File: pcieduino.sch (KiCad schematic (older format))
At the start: 32 parts, among them IC1 ATMEGA328P-A, J1 PCIE-MINI, J2 ANALOG, J3 ISP, J4 POWER, J5 DIGITAL, SW1 SW_PUSH, U1 MCP2200, X1 12MHz, X2 8MHz

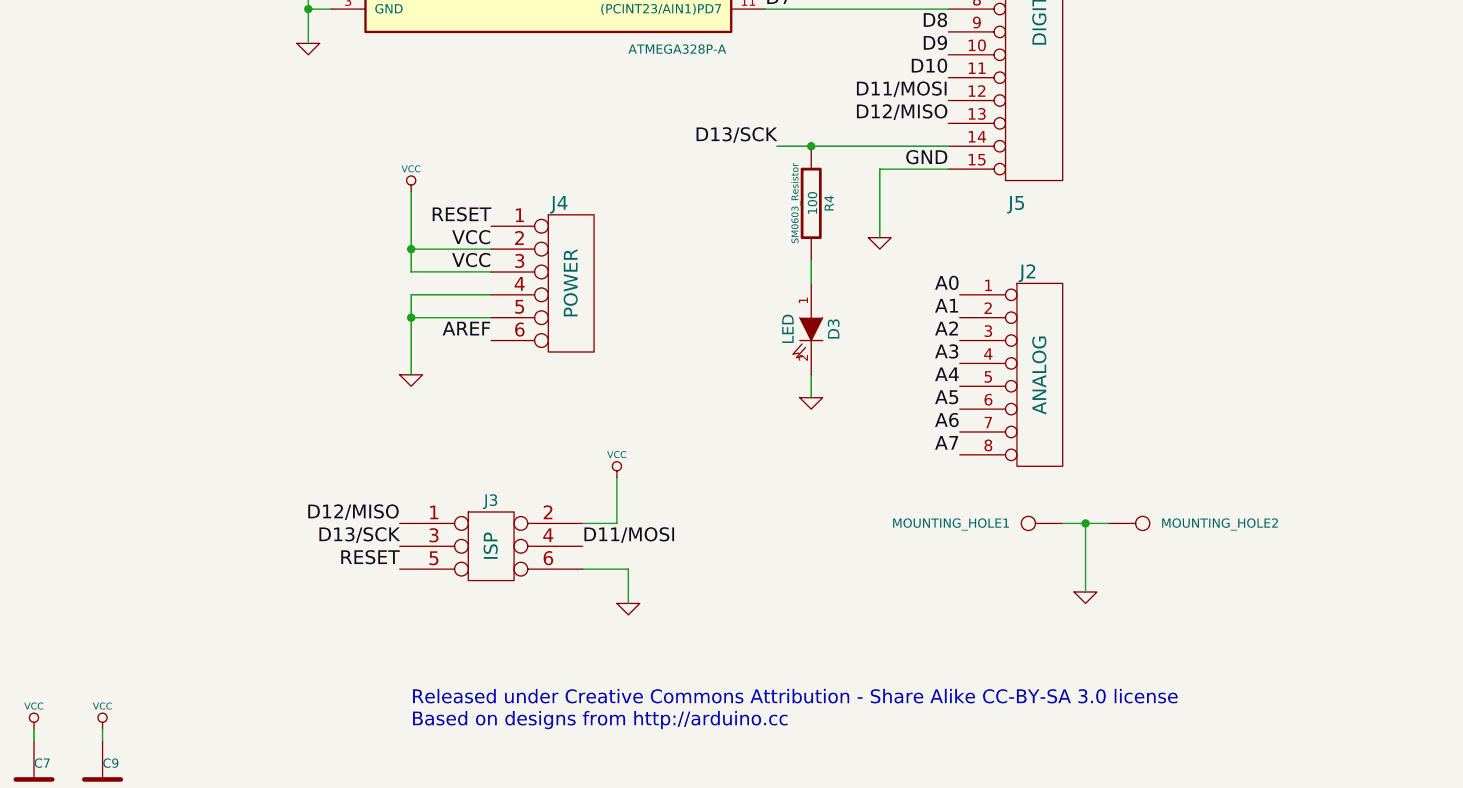
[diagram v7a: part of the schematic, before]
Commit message: add 01/04 changes
summary:

* redrawn the board starting from x=100.00, y=100.00 to have fix positioning
* combine analog and power headers
* remove RESET from power header because it already exists elsewhere
* redraw fill zones with duplication
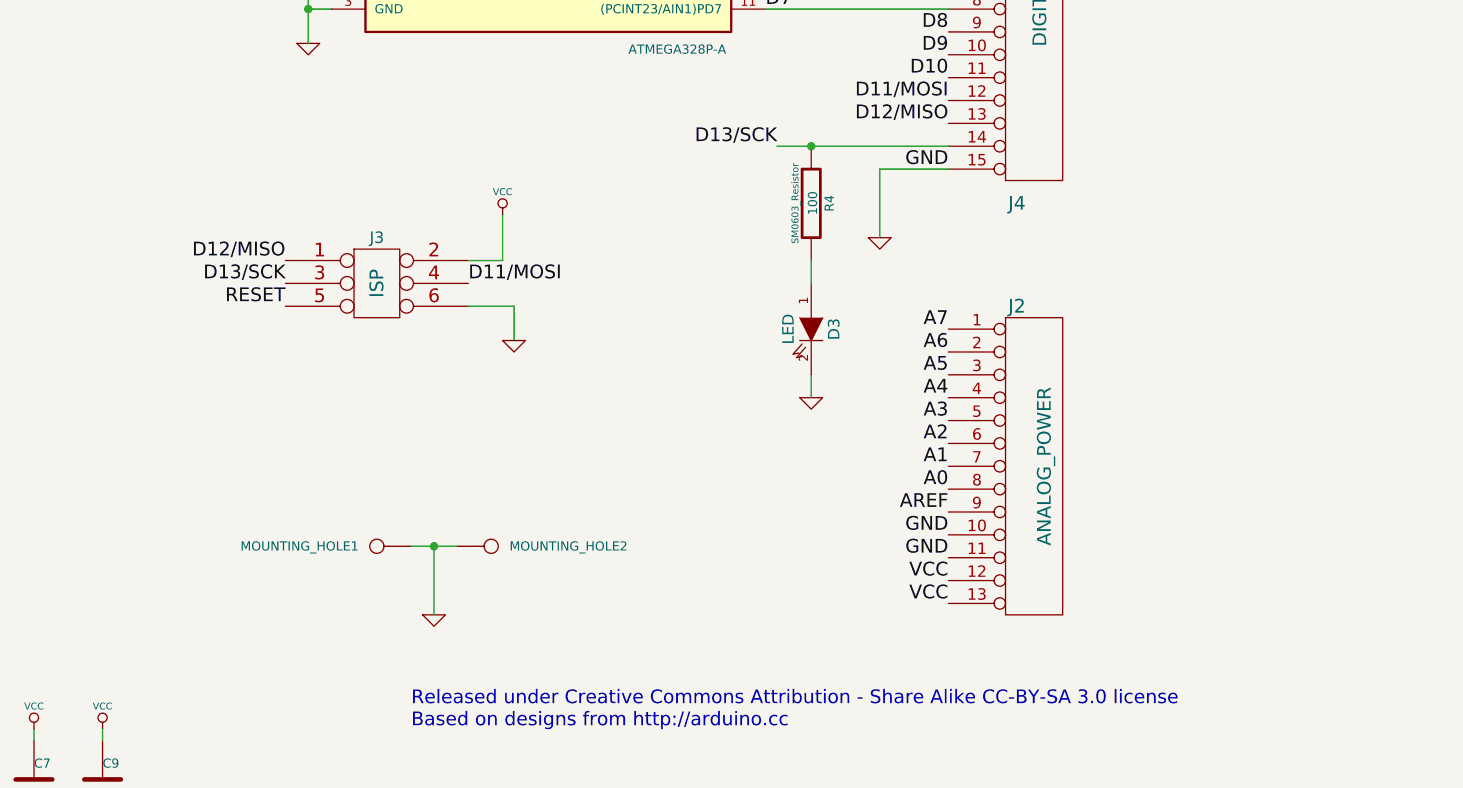
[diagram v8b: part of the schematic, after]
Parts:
- removed J2: ANALOG, ~, symbol CONN_8
- removed J4: POWER, ~, symbol CONN_6
- added J2: ANALOG_POWER, ~, symbol CONN_13
- renumbered J5 to J4
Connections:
- net A0: now also J2.8 (P8)
- net A1: now also J2.7 (P7)
- net A2: now also J2.6 (P6)
- net A3: now also J2.5 (P5)
- net A4: now also J2.4 (P4)
- net A5: now also J2.3 (P3)
- net A6: now also J2.2 (P2)
- net A7: now also J2.1 (P1)
- net AREF: now also J2.9 (P9)
- net GND: now also J2.10 (P10), J2.11 (P11)
- net VCC: now also J2.12 (P12), J2.13 (P13)
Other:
- moved on the sheet: J3, MOUNTING_HOLE1, MOUNTING_HOLE2
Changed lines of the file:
@@
 Sheet 1 1
 Title "PCIeDuino328v1"
-Date "3 jan 2015"
+Date "4 jan 2015"
 Rev "1"
 Comp "moonpunch.org"
@@
 L CONN_3X2 J3
 U 1 1 53F9FD80
-P 7500 6050
-F 0 "J3" H 7500 6300 50  0000 C CNN
-F 1 "ISP" V 7500 6100 60  0000 C CNN
-F 2 "~" H 7500 6050 60  0000 C CNN
-F 3 "~" H 7500 6050 60  0000 C CNN
-	1    7500 6050
+P 7000 4900
+F 0 "J3" H 7000 5150 50  0000 C CNN
+F 1 "ISP" V 7000 4950 60  0000 C CNN
+F 2 "~" H 7000 4900 60  0000 C CNN
+F 3 "~" H 7000 4900 60  0000 C CNN
+	1    7000 4900
 	1    0    0    -1
 $EndComp
@@
 L GND #PWR08
 U 1 1 53F9FDA8
-P 8100 6250
-F 0 "#PWR08" H 8100 6250 30  0001 C CNN
-F 1 "GND" H 8100 6180 30  0001 C CNN
-F 2 "" H 8100 6250 60  0000 C CNN
-F 3 "" H 8100 6250 60  0000 C CNN
-	1    8100 6250
-	1    0    0    -1
-$EndComp
-Text Label 7100 5900 2    60   ~ 0
+P 7600 5100
+F 0 "#PWR08" H 7600 5100 30  0001 C CNN
+F 1 "GND" H 7600 5030 30  0001 C CNN
+F 2 "" H 7600 5100 60  0000 C CNN
+F 3 "" H 7600 5100 60  0000 C CNN
+	1    7600 5100
+	1    0    0    -1
+$EndComp
+Text Label 6600 4750 2    60   ~ 0
 D12/MISO
-Text Label 7100 6000 2    60   ~ 0
+Text Label 6600 4850 2    60   ~ 0
 D13/SCK
-Text Label 7900 6000 0    60   ~ 0
+Text Label 7400 4850 0    60   ~ 0
 D11/MOSI
 $Comp
 L VCC #PWR09
 U 1 1 53F9FDFE
-P 8050 5700
-F 0 "#PWR09" H 8050 5800 30  0001 C CNN
-F 1 "VCC" H 8050 5800 30  0000 C CNN
-F 2 "" H 8050 5700 60  0000 C CNN
-F 3 "" H 8050 5700 60  0000 C CNN
-	1    8050 5700
-	1    0    0    -1
-$EndComp
-Text Label 7100 6100 2    60   ~ 0
+P 7550 4550
+F 0 "#PWR09" H 7550 4650 30  0001 C CNN
+F 1 "VCC" H 7550 4650 30  0000 C CNN
+F 2 "" H 7550 4550 60  0000 C CNN
+F 3 "" H 7550 4550 60  0000 C CNN
+	1    7550 4550
+	1    0    0    -1
+$EndComp
+Text Label 6600 4950 2    60   ~ 0
 RESET
 $Comp
@@
 	0    -1   -1   0
 $EndComp
-$Comp
-L CONN_6 J4
-U 1 1 53FA0B3F
-P 7850 4850
-F 0 "J4" H 7800 5200 60  0000 C CNN
-F 1 "POWER" V 7850 4850 60  0000 C CNN
-F 2 "~" H 7850 4850 60  0000 C CNN
-F 3 "~" H 7850 4850 60  0000 C CNN
-	1    7850 4850
-	1    0    0    -1
-$EndComp
-Text Label 7500 4600 2    60   ~ 0
-RESET
-Text Label 7500 4700 2    60   ~ 0
+Text Label 9500 6150 2    60   ~ 0
 VCC
-Text Label 7500 4800 2    60   ~ 0
+Text Label 9500 6250 2    60   ~ 0
 VCC
-$Comp
-L VCC #PWR014
-U 1 1 53FA0B7B
-P 7150 4450
-F 0 "#PWR014" H 7150 4550 30  0001 C CNN
-F 1 "VCC" H 7150 4550 30  0000 C CNN
-F 2 "" H 7150 4450 60  0000 C CNN
-F 3 "" H 7150 4450 60  0000 C CNN
-	1    7150 4450
-	1    0    0    -1
-$EndComp
-$Comp
-L GND #PWR015
-U 1 1 53FA0C39
-P 7150 5250
-F 0 "#PWR015" H 7150 5250 30  0001 C CNN
-F 1 "GND" H 7150 5180 30  0001 C CNN
-F 2 "" H 7150 5250 60  0000 C CNN
-F 3 "" H 7150 5250 60  0000 C CNN
-	1    7150 5250
-	1    0    0    -1
-$EndComp
 Text Label 9500 3750 2    60   ~ 0
 D8
@@
 D12/MISO
 $Comp
-L GND #PWR016
+L GND #PWR014
 U 1 1 53FA0D4F
 P 9200 4650
-F 0 "#PWR016" H 9200 4650 30  0001 C CNN
+F 0 "#PWR014" H 9200 4650 30  0001 C CNN
 F 1 "GND" H 9200 4580 30  0001 C CNN
 F 2 "" H 9200 4650 60  0000 C CNN
@@
 $EndComp
 $Comp
-L GND #PWR017
+L GND #PWR015
 U 1 1 53FA0DE1
 P 8900 5350
-F 0 "#PWR017" H 8900 5350 30  0001 C CNN
+F 0 "#PWR015" H 8900 5350 30  0001 C CNN
 F 1 "GND" H 8900 5280 30  0001 C CNN
 F 2 "" H 8900 5350 60  0000 C CNN
@@
 $EndComp
 $Comp
-L GND #PWR018
+L GND #PWR016
 U 1 1 53FA0F93
 P 5800 7300
-F 0 "#PWR018" H 5800 7300 30  0001 C CNN
+F 0 "#PWR016" H 5800 7300 30  0001 C CNN
 F 1 "GND" H 5800 7230 30  0001 C CNN
 F 2 "" H 5800 7300 60  0000 C CNN
@@
 $EndComp
 $Comp
-L VCC #PWR019
+L VCC #PWR017
 U 1 1 53FA0FA2
 P 5800 6800
-F 0 "#PWR019" H 5800 6900 30  0001 C CNN
+F 0 "#PWR017" H 5800 6900 30  0001 C CNN
 F 1 "VCC" H 5800 6900 30  0000 C CNN
 F 2 "" H 5800 6800 60  0000 C CNN
@@
 $EndComp
 $Comp
-L PWR_FLAG #FLG020
+L PWR_FLAG #FLG018
 U 1 1 53FA0835
 P 4350 6900
-F 0 "#FLG020" H 4350 6995 30  0001 C CNN
+F 0 "#FLG018" H 4350 6995 30  0001 C CNN
 F 1 "PWR_FLAG" H 4350 7080 30  0000 C CNN
 F 2 "" H 4350 6900 60  0000 C CNN
@@
 $EndComp
 $Comp
-L PWR_FLAG #FLG021
+L PWR_FLAG #FLG019
 U 1 1 53FF089D
 P 3400 7200
-F 0 "#FLG021" H 3400 7295 30  0001 C CNN
+F 0 "#FLG019" H 3400 7295 30  0001 C CNN
 F 1 "PWR_FLAG" H 3400 7380 30  0000 C CNN
 F 2 "" H 3400 7200 60  0000 C CNN
@@
 $EndComp
 $Comp
-L GND #PWR022
+L GND #PWR020
 U 1 1 53FF08AC
 P 3600 7250
-F 0 "#PWR022" H 3600 7250 30  0001 C CNN
+F 0 "#PWR020" H 3600 7250 30  0001 C CNN
 F 1 "GND" H 3600 7180 30  0001 C CNN
 F 2 "" H 3600 7250 60  0000 C CNN
@@
 	1    0    0    -1
 $EndComp
-Text Label 7500 5100 2    60   ~ 0
+Text Label 9500 5850 2    60   ~ 0
 AREF
 $Comp
@@
 $EndComp
 $Comp
-L VCC #PWR023
+L VCC #PWR021
 U 1 1 549E6F8C
 P 2700 1000
-F 0 "#PWR023" H 2700 1100 30  0001 C CNN
+F 0 "#PWR021" H 2700 1100 30  0001 C CNN
 F 1 "VCC" H 2700 1100 30  0000 C CNN
 F 2 "" H 2700 1000 60  0000 C CNN
@@
 	4300 6900 4550 6900
 Wire Wire Line
-	7900 6100 8100 6100
-Wire Wire Line
-	8100 6100 8100 6250
-Wire Wire Line
-	7900 5900 8050 5900
-Wire Wire Line
-	8050 5900 8050 5700
+	7400 4950 7600 4950
+Wire Wire Line
+	7600 4950 7600 5100
+Wire Wire Line
+	7400 4750 7550 4750
+Wire Wire Line
+	7550 4750 7550 4550
 Wire Wire Line
 	5200 7250 5200 7300
@@
 Wire Wire Line
 	9600 1950 9600 1350
-Wire Wire Line
-	7150 4450 7150 4800
-Wire Wire Line
-	7150 4800 7500 4800
-Wire Wire Line
-	7500 4700 7150 4700
-Connection ~ 7150 4700
-Wire Wire Line
-	7150 5250 7150 4900
-Wire Wire Line
-	7150 4900 7500 4900
-Wire Wire Line
-	7500 5000 7150 5000
-Connection ~ 7150 5000
 Wire Wire Line
 	9200 4650 9200 4350
@@
 Connection ~ 2150 2200
 $Comp
-L GND #PWR024
+L GND #PWR022
 U 1 1 549E739D
 P 1850 2900
-F 0 "#PWR024" H 1850 2900 30  0001 C CNN
+F 0 "#PWR022" H 1850 2900 30  0001 C CNN
 F 1 "GND" H 1850 2830 30  0001 C CNN
 F 2 "" H 1850 2900 60  0000 C CNN
@@
 USB_M
 $Comp
-L VCC #PWR025
+L VCC #PWR023
 U 1 1 549E7653
 P 5200 2150
-F 0 "#PWR025" H 5200 2250 30  0001 C CNN
+F 0 "#PWR023" H 5200 2250 30  0001 C CNN
 F 1 "VCC" H 5200 2250 30  0000 C CNN
 F 2 "" H 5200 2150 60  0000 C CNN
@@
 $EndComp
 $Comp
-L VCC #PWR026
+L VCC #PWR024
 U 1 1 549E7797
 P 2550 3700
-F 0 "#PWR026" H 2550 3800 30  0001 C CNN
+F 0 "#PWR024" H 2550 3800 30  0001 C CNN
 F 1 "VCC" H 2550 3800 30  0000 C CNN
 F 2 "" H 2550 3700 60  0000 C CNN
@@
 Connection ~ 2550 3700
 $Comp
-L GND #PWR027
+L GND #PWR025
 U 1 1 549E7B0D
 P 5350 1800
-F 0 "#PWR027" H 5350 1800 30  0001 C CNN
+F 0 "#PWR025" H 5350 1800 30  0001 C CNN
 F 1 "GND" H 5350 1730 30  0001 C CNN
 F 2 "" H 5350 1800 60  0000 C CNN
@@
 Connection ~ 1850 2850
 $Comp
-L GND #PWR028
+L GND #PWR026
 U 1 1 54A7DBD9
-P 10100 6200
-F 0 "#PWR028" H 10100 6200 30  0001 C CNN
-F 1 "GND" H 10100 6130 30  0001 C CNN
-F 2 "" H 10100 6200 60  0000 C CNN
-F 3 "" H 10100 6200 60  0000 C CNN
-	1    10100 6200
+P 7250 6300
+F 0 "#PWR026" H 7250 6300 30  0001 C CNN
+F 1 "GND" H 7250 6230 30  0001 C CNN
+F 2 "" H 7250 6300 60  0000 C CNN
+F 3 "" H 7250 6300 60  0000 C CNN
+	1    7250 6300
 	1    0    0    -1
 $EndComp
@@
 L CONN_1 MOUNTING_HOLE2
 U 1 1 54A7DBE8
-P 10350 5900
-F 0 "MOUNTING_HOLE2" H 10430 5900 40  0000 L CNN
-F 1 "CONN_1" H 10350 5955 30  0001 C CNN
-F 2 "~" H 10350 5900 60  0000 C CNN
-F 3 "~" H 10350 5900 60  0000 C CNN
-	1    10350 5900
+P 7500 6000
+F 0 "MOUNTING_HOLE2" H 7580 6000 40  0000 L CNN
+F 1 "CONN_1" H 7500 6055 30  0001 C CNN
+F 2 "~" H 7500 6000 60  0000 C CNN
+F 3 "~" H 7500 6000 60  0000 C CNN
+	1    7500 6000
 	1    0    0    -1
 $EndComp
@@
 L CONN_1 MOUNTING_HOLE1
 U 1 1 54A7DBF7
-P 9850 5900
-F 0 "MOUNTING_HOLE1" H 9930 5900 40  0000 L CNN
-F 1 "CONN_1" H 9850 5955 30  0001 C CNN
-F 2 "~" H 9850 5900 60  0000 C CNN
-F 3 "~" H 9850 5900 60  0000 C CNN
-	1    9850 5900
+P 7000 6000
+F 0 "MOUNTING_HOLE1" H 7080 6000 40  0000 L CNN
+F 1 "CONN_1" H 7000 6055 30  0001 C CNN
+F 2 "~" H 7000 6000 60  0000 C CNN
+F 3 "~" H 7000 6000 60  0000 C CNN
+	1    7000 6000
 	-1   0    0    1
 $EndComp
 Wire Wire Line
-	10000 5900 10200 5900
-Wire Wire Line
-	10100 5900 10100 6200
-Connection ~ 10100 5900
-$Comp
-L CONN_15 J5
+	7150 6000 7350 6000
+Wire Wire Line
+	7250 6000 7250 6300
+Connection ~ 7250 6000
+$Comp
+L CONN_15 J4
 U 1 1 54A7E504
 P 9850 3650
-F 0 "J5" H 9800 2800 60  0000 C CNN
+F 0 "J4" H 9800 2800 60  0000 C CNN
 F 1 "DIGITAL" V 9900 3650 60  0000 C CNN
 F 2 "~" H 9850 3700 60  0000 C CNN
@@
 Text Label 6800 2800 2    60   ~ 0
 A7
-$Comp
-L CONN_8 J2
-U 1 1 54A7F47E
-P 9900 5250
-F 0 "J2" H 9850 5700 60  0000 C CNN
-F 1 "ANALOG" V 9900 5250 60  0000 C CNN
-F 2 "~" H 9900 5250 60  0000 C CNN
-F 3 "~" H 9900 5250 60  0000 C CNN
-	1    9900 5250
-	1    0    0    -1
-$EndComp
-Text Label 9550 4900 2    60   ~ 0
+Text Label 9500 5750 2    60   ~ 0
 A0
-Text Label 9550 5000 2    60   ~ 0
+Text Label 9500 5650 2    60   ~ 0
 A1
-Text Label 9550 5100 2    60   ~ 0
+Text Label 9500 5550 2    60   ~ 0
 A2
-Text Label 9550 5200 2    60   ~ 0
+Text Label 9500 5450 2    60   ~ 0
 A3
-Text Label 9550 5300 2    60   ~ 0
+Text Label 9500 5350 2    60   ~ 0
 A4
-Text Label 9550 5400 2    60   ~ 0
+Text Label 9500 5250 2    60   ~ 0
 A5
-Text Label 9550 5500 2    60   ~ 0
+Text Label 9500 5150 2    60   ~ 0
 A6
-Text Label 9550 5600 2    60   ~ 0
+Text Label 9500 5050 2    60   ~ 0
 A7
+Text Label 9500 5950 2    60   ~ 0
+GND
+Text Label 9500 6050 2    60   ~ 0
+GND
+$Comp
+L CONN_13 J2
+U 1 1 54A91C6A
+P 9850 5650
+F 0 "J2" H 9800 6350 60  0000 C CNN
+F 1 "ANALOG_POWER" V 9920 5650 60  0000 C CNN
+F 2 "~" H 9850 5650 60  0000 C CNN
+F 3 "~" H 9850 5650 60  0000 C CNN
+	1    9850 5650
+	1    0    0    -1
+$EndComp
 $EndSCHEMATC
